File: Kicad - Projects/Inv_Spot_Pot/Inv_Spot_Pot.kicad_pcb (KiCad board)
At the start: 2 copper layers, 179.5 x 190 mm, 105 parts, among them J2 PWM, J3 Display_Power, J4 24V, J5 24V, K1 Y14x-1C-xxDS, Q1 60N60, Q2 60N60, Q3 60N60, Q4 60N60, T1 Transformer_1P_2S, U2 LTV-817S

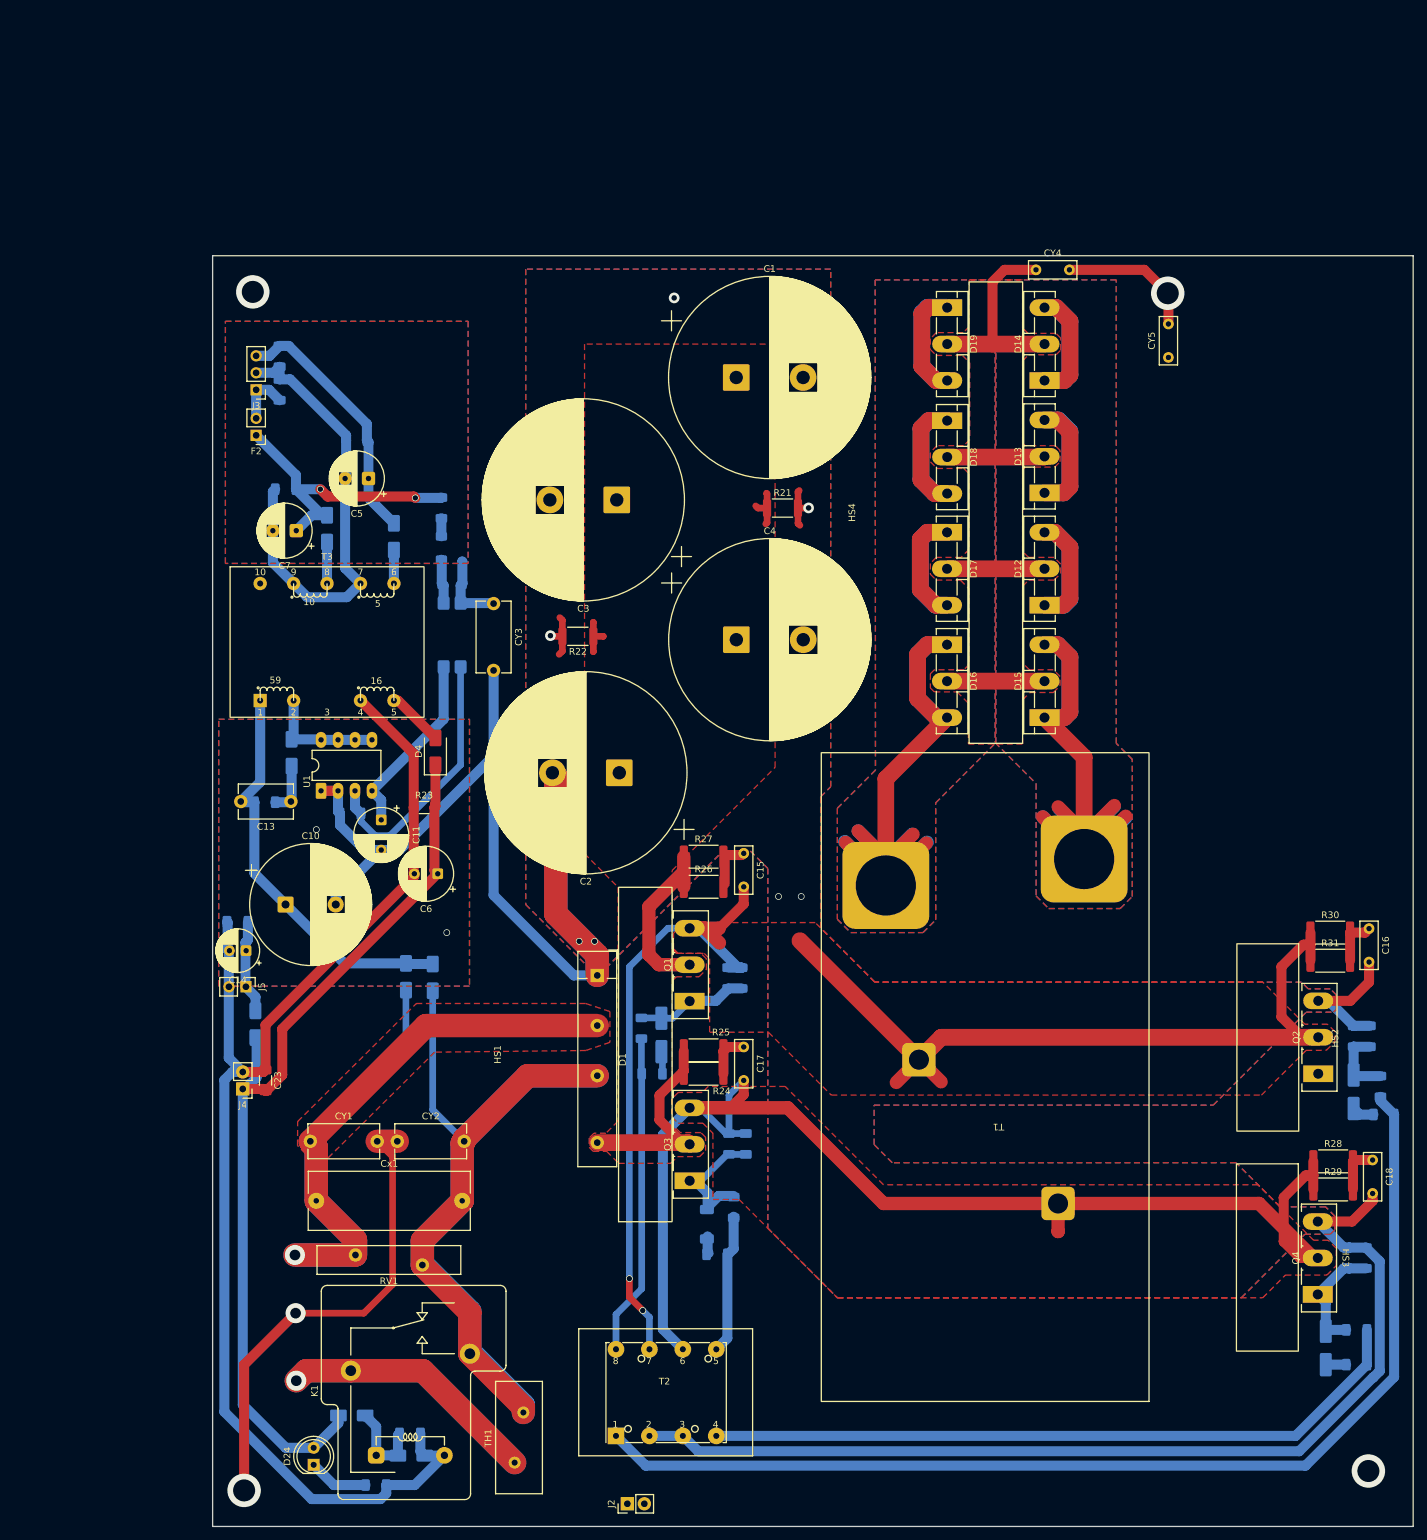
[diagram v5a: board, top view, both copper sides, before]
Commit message: Melhoras na Placa de Potência
Melhor espalhamento do plano Earth

Conexões melhores entre os planos e os componentes
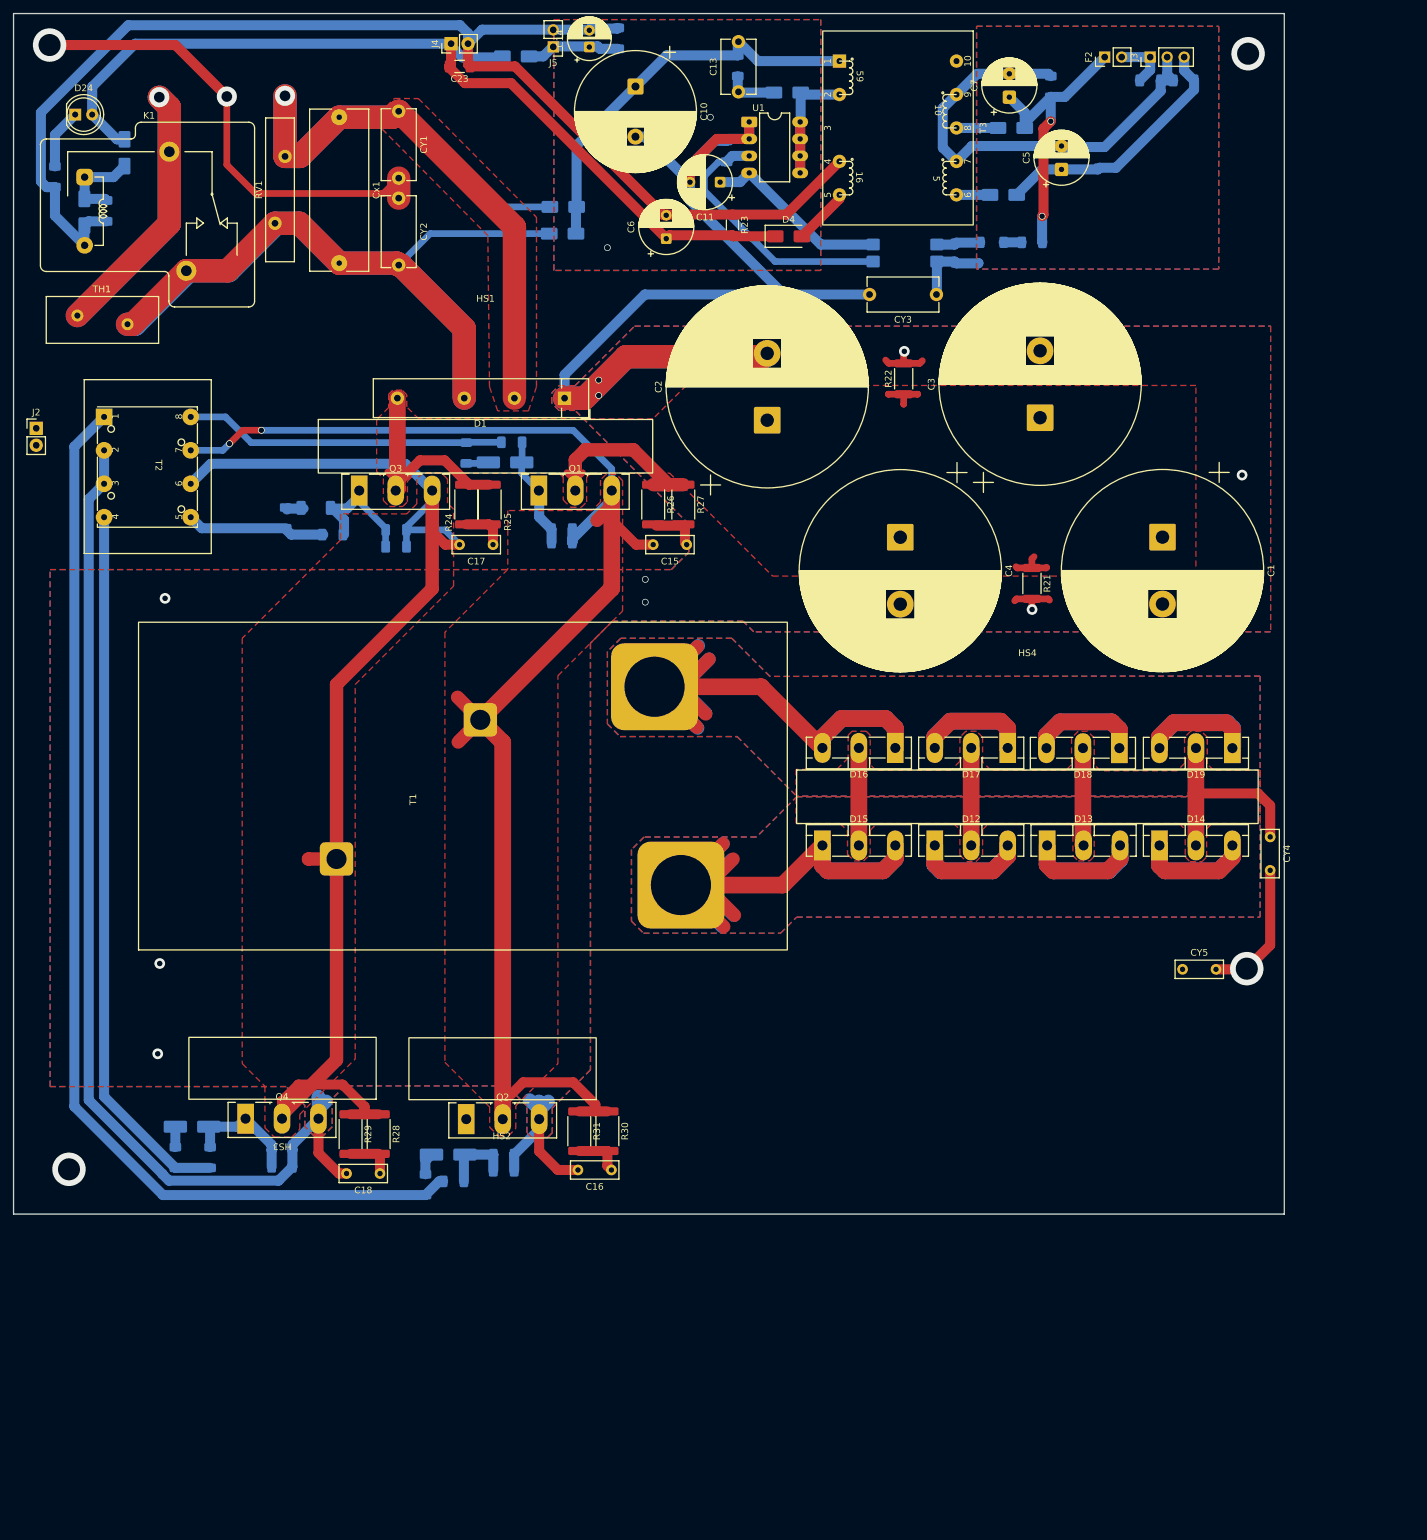
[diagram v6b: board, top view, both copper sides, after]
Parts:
- moved D24 205.0 mm to (23.9, 28.1), turned to 0 degrees
- moved R9 201.4 mm to (20.8, 37.4), turned to -90 degrees
- moved K1 195.4 mm to (22.7, 42.5), turned to 0 degrees
- moved D22 192.2 mm to (25.2, 42.7), turned to -90 degrees
- moved D23 191.8 mm to (31.2, 33.8), turned to 90 degrees
- moved C24 188.4 mm to (28.5, 42.5), turned to 90 degrees
- moved TH1 183.6 mm to (24.2, 58.1), turned to 0 degrees
- moved J2 183.5 mm to (18.0, 75.0), turned to 0 degrees
- moved R19 179.3 mm to (38.8, 184.0), turned to -90 degrees
- moved R20 173.3 mm to (44.0, 184.0), turned to -90 degrees
- moved D11 172.7 mm to (41.3, 179.4), turned to 0 degrees
- moved RV1 164.6 mm to (55.2, 34.3), turned to -90 degrees
- moved HS3 164.2 mm to (54.9, 187.2), turned to 180 degrees
- moved R16 162.6 mm to (54.8, 185.4), turned to 180 degrees
- moved Q4 162.5 mm to (49.3, 178.2), turned to 0 degrees
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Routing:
- net Earth: track 361.4 -> 390.1 mm, vias 9 -> 12
- net T-: track 219.6 -> 236.8 mm
- net 310V: track 70.4 -> 80.0 mm
- net Net-(D3-A): track 18.0 -> 25.6 mm
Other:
- board size 179.5 x 190 mm -> 190 x 179.5 mm

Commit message: Preparação para Manufatura
Validação de footprints

Serigrafia movida para melhorar legibilidade

Backup de versão com trafo anterior salvo

Adição de snippet de código para ativação da proteção térmica
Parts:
- removed CY5: C, Capacitor_THT:C_Disc_D7.0mm_W2.5mm_P5.00mm
- added H1: MountingHole_Pad, Board_Fixation:Hexagonal-M3-Padded, F.Cu at (19.1, 38.0)
- added H10: MountingHole_Pad, MountingHole:MountingHole_3.2mm_M3_Pad_TopOnly, F.Cu at (54.8, 171.3)
- added H2: MountingHole_Pad, Board_Fixation:Hexagonal-M3-Padded, F.Cu at (190.8, 170.2)
- added H3: MountingHole, Board_Fixation:Hexagonal-M3, F.Cu at (24.0, 179.5)
- added H4: MountingHole, Board_Fixation:Hexagonal-M3, F.Cu at (198.7, 37.7)
- added H9: MountingHole_Pad, MountingHole:MountingHole_3.2mm_M3_Pad_TopOnly, F.Cu at (87.8, 171.5)
- added J6: PWM, Connector_PinHeader_2.54mm:PinHeader_1x02_P2.54mm_Vertical, F.Cu at (17.4, 70.3)
- CY1, CY2, CY3: footprint Capacitor_THT:C_Disc_D10.5mm_W5.0mm_P10.00mm -> Capacitor_THT:C_Disc_D10.5mm_W5.0mm_P7.50mm
- CY4: footprint Capacitor_THT:C_Disc_D7.0mm_W2.5mm_P5.00mm -> Capacitor_THT:C_Disc_D10.5mm_W5.0mm_P7.50mm
- D1: value KBU4M -> HD50SB100
- R1, R17, R19, R5: value 2 -> 5.1
- R12, R8: value 2k -> 2k2
- R18, R2, R20, R6: value 27 -> 15
- T3: footprint Transformer_THT:Transformer_Breve_TEZ-28x33 -> Custom_Transformer:EE25V-8T
- moved T3 22.3 mm to (159.0, 27.7)
- moved J2 13.9 mm to (17.4, 88.9), turned to 90 degrees
- moved R18 7.30 mm to (59.5, 84.1)
- moved CY2 5.06 mm to (76.8, 42.8)
- moved Cx1 4.57 mm to (67.9, 28.1)
- moved C24 4.57 mm to (33.1, 42.5)
- moved D22 4.57 mm to (29.8, 42.7)
- moved D24 4.57 mm to (28.4, 28.1)
- moved K1 4.57 mm to (27.3, 42.5)
- moved R9 4.57 mm to (25.4, 37.4)
- moved RV1 4.57 mm to (59.8, 34.3)
- moved TH1 4.57 mm to (28.8, 58.1)
- moved D23 4.57 mm to (35.8, 33.8)
- moved CY1 4.57 mm to (76.8, 27.6)
- moved D6 3.77 mm to (162.6, 36.3)
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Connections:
- D1 pad 1: Earth -> 310V
- D1 pad 4: 310V -> Earth
- T3 pad 4: GND_{24} -> Net-(D4-A)
- T3 pad 5: Net-(D4-A) -> Net-(D6-A)
- T3 pad 6: Net-(D6-A) -> GND
- T3 pad 7: GND -> Net-(D5-A)
- T3 pad 8: Net-(D5-A) -> GND
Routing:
- net Earth_Protective: track 92.1 -> 181.6 mm, vias 5 -> 1
- net Earth: track 390.1 -> 332.3 mm, vias 12 -> 57
- net /Soft_Start-24V/~{AC{1}}: track 171.8 -> 141.1 mm
- net GND: track 80.9 -> 59.1 mm
- net /PWM_L: track 0.00 -> 18.6 mm
- net /PWM_H: track 0.00 -> 18.6 mm
- net 24V: track 139.0 -> 128.1 mm
- net GND_{24}: track 196.0 -> 204.3 mm, vias 0 -> 1
- net Net-(D4-A): track 8.52 -> 16.1 mm, vias 0 -> 1
- net T+: track 198.3 -> 192.3 mm
- net T-: track 236.8 -> 242.0 mm, vias 2 -> 0
- net /Soft_Start-24V/AC_{2}: track 136.3 -> 131.3 mm
- net 310V: track 80.0 -> 75.6 mm
- net Net-(D5-A): track 6.20 -> 9.96 mm
- net Net-(D6-A): track 5.00 -> 7.89 mm
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- added copper zone on F.Cu, net /Soft_Start-24V/~{AC{1}}
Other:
- board text added: "15V"
- board text added: "24V"
- board text added: "24V Cooler"
- board text added: "7V"
- board text added: "Proteção Térmica"
- board text added: "Spotcar Inversora Placa de Potência Rev 07/10/2026 - V1.0.0"

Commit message: Toques Finais
Ajustes finais antes da produção
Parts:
- CY1, CY2, CY3, CY4: footprint Capacitor_THT:C_Disc_D10.5mm_W5.0mm_P7.50mm -> Custom_Capacitors:C_Disc_D7.0mm_W2.5mm_P7.50mm
- D7: value BZV55B15 -> BZV55B12
- moved R13 14.6 mm to (59.6, 82.0), turned to -90 degrees
- moved C22 14.4 mm to (62.1, 82.0), turned to 90 degrees
- moved C20 13.0 mm to (95.4, 77.1)
- moved R3 13.0 mm to (95.4, 79.1)
- moved CY1 4.02 mm to (76.8, 31.6)
- moved CY2 3.84 mm to (76.8, 46.6)
- moved CY4 3.77 mm to (202.5, 139.8)
- moved CY3 3.75 mm to (148.9, 55.0)
- moved R18 3.51 mm to (56.0, 84.1)
- moved R17 1.69 mm to (54.4, 87.0), turned to 180 degrees
- moved D10 0.41 mm to (60.2, 86.9)
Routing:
- net T+: track 192.3 -> 173.5 mm
- net ~{Gate}: track 10.7 -> 16.1 mm
- net T-: track 242.0 -> 237.6 mm
- net PWM1: track 18.7 -> 15.8 mm
- net Gate1: track 18.5 -> 20.2 mm
- net Earth: track 332.3 -> 334.0 mm, vias 57 -> 152
- net Gate: track 16.9 -> 15.3 mm
- net 310V: track 75.6 -> 74.5 mm
